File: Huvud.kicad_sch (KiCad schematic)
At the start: 117 parts, among them J10 Probe, J12 5V, J2 DBG, J3 THERM, J4 FAN0, J5 FAN1, J6 Heater, J7 Endstop, J9 STEPPER, Q1 AO3400A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

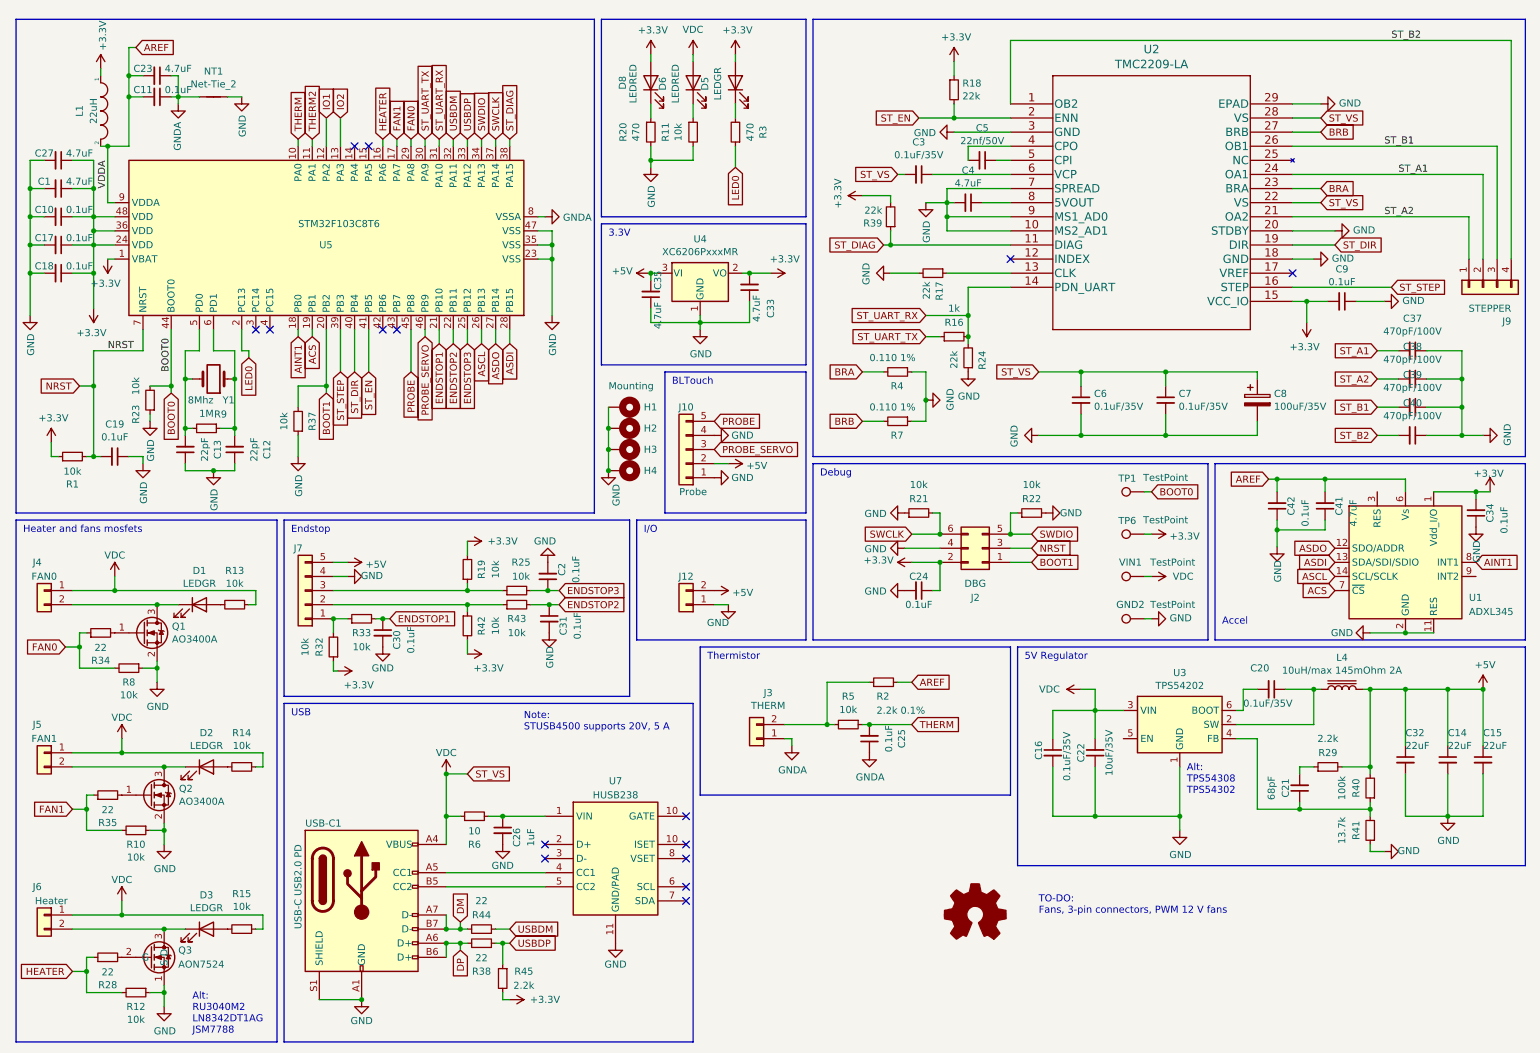
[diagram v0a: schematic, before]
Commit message: repace TMC2209 with module
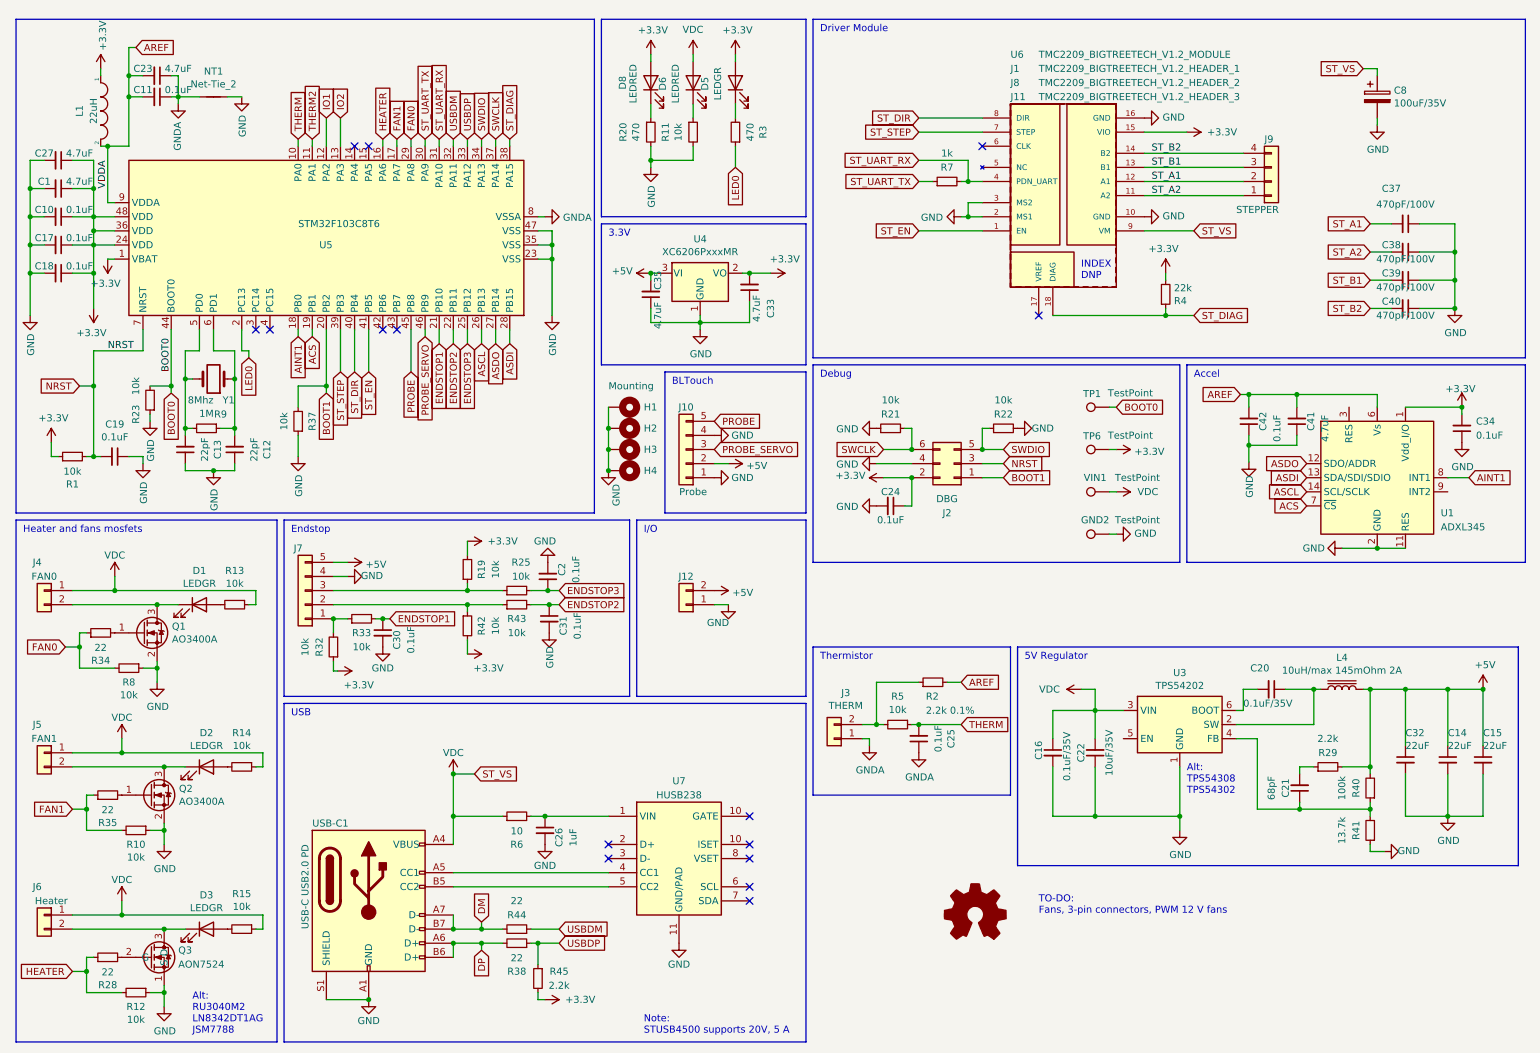
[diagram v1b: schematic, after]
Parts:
- removed C3, C6, C7: 0.1uF/35V, Capacitor_SMD:C_0603_1608Metric, symbol Device:C_Small
- removed C4: 4.7uF, Capacitor_SMD:C_0402_1005Metric, symbol Device:C_Small
- removed C5: 22nf/50V, Capacitor_SMD:C_0603_1608Metric, symbol Device:C_Small
- removed C9: 0.1uF, Capacitor_SMD:C_0402_1005Metric, symbol Device:C_Small
- removed R16: 1k, Resistor_SMD:R_0402_1005Metric, symbol Device:R_Small
- removed R17, R18, R24, R39: 22k, Resistor_SMD:R_0402_1005Metric, symbol Device:R_Small
- removed U2: TMC2209-LA, TMC2209:TMC2209-LA, symbol TMC2209:TMC2209-LA
- added J1: TMC2209_BIGTREETECH_V1.2_HEADER_1, Huvud:HEADER_TMC2209_BIGTREETECH_1, symbol Huvud:TMC2209_BIGTREETECH_V1.2_HEADER_1
- added J11: TMC2209_BIGTREETECH_V1.2_HEADER_3, Huvud:HEADER_TMC2209_BIGTREETECH_3, symbol Huvud:TMC2209_BIGTREETECH_V1.2_HEADER_3
- added J8: TMC2209_BIGTREETECH_V1.2_HEADER_2, Huvud:HEADER_TMC2209_BIGTREETECH_2, symbol Huvud:TMC2209_BIGTREETECH_V1.2_HEADER_2
- added U6: TMC2209_BIGTREETECH_V1.2_MODULE, Huvud:MODULE_TMC2209_BIGTREETECH, symbol Huvud:TMC2209_BIGTREETECH_V1.2_MODULE
- R4: value 0.110 1% -> 22k; footprint Resistor_SMD:R_1206_3216Metric -> Resistor_SMD:R_0402_1005Metric; LCSC (none) -> C25768
- R7: value 0.110 1% -> 1k; footprint Resistor_SMD:R_1206_3216Metric -> Resistor_SMD:R_0402_1005Metric; LCSC (none) -> C21190
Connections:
- net BRA is gone; now on net +3V3: R4.2
- net BRB is gone; now on net ST_UART_RX: R7.2
- net +3V3: now also J8.15 (VIO)
- net GND: now also J1.2 (MS1), J1.3 (MS2), J8.10 (GND), J8.16 (GND); no longer R4.1, R7.1
- net ST_A1: now also J8.12 (A1)
- net ST_A2: now also J8.11 (A2)
- net ST_B1: now also J8.13 (B1)
- net ST_B2: now also J8.14 (B2)
- net ST_DIAG: now also R4.1, J11.18 (DIAG)
- net ST_DIR: now also J1.8 (DIR)
- net ST_EN: now also J1.1 (EN)
- net ST_STEP: now also J1.7 (STEP)
- net ST_UART_RX: now also J1.4 (PDN_UART)
- net ST_UART_TX: now also R7.1
- net VDC: now also J8.9 (VM)
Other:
- note added: "Driver Module"
- note added: "INDEX DNP"
- moved on the sheet: C24, C25, C26, C34, C37, C38, C39, C40, C41, C42, C8, GND2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

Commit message: cleanup and bom
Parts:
- GND2, H1, H2, H3, H4, TP1, TP6, VIN1: now left out of the parts list
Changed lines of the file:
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@@
   )
   (symbol (lib_id "Mechanical:MountingHole_Pad") (at 121.92 82.55 270) (unit 1)
-    (in_bom yes) (on_board yes) (dnp no)
+    (in_bom no) (on_board yes) (dnp no)
     (property "Reference" "H1" (at 125.73 82.55 90)
       (effects (font (size 1.27 1.27)) (justify left))
@@
   )
   (symbol (lib_id "Mechanical:MountingHole_Pad") (at 121.92 86.36 270) (unit 1)
-    (in_bom yes) (on_board yes) (dnp no)
+    (in_bom no) (on_board yes) (dnp no)
     (property "Reference" "H2" (at 125.73 86.36 90)
       (effects (font (size 1.27 1.27)) (justify left))
@@
   )
   (symbol (lib_id "Mechanical:MountingHole_Pad") (at 121.92 90.17 270) (unit 1)
-    (in_bom yes) (on_board yes) (dnp no)
+    (in_bom no) (on_board yes) (dnp no)
     (property "Reference" "H3" (at 125.73 90.17 90)
       (effects (font (size 1.27 1.27)) (justify left))
@@
   )
   (symbol (lib_id "Mechanical:MountingHole_Pad") (at 121.92 93.98 270) (unit 1)
-    (in_bom yes) (on_board yes) (dnp no)
+    (in_bom no) (on_board yes) (dnp no)
     (property "Reference" "H4" (at 125.73 93.98 90)
       (effects (font (size 1.27 1.27)) (justify left))
@@
   )
   (symbol (lib_id "Connector:TestPoint") (at 209.55 82.55 90) (unit 1)
-    (in_bom yes) (on_board yes) (dnp no)
+    (in_bom no) (on_board yes) (dnp no)
     (property "Reference" "TP1" (at 206.4512 80.137 90)
       (effects (font (size 1.27 1.27)))
@@
   )
   (symbol (lib_id "Connector:TestPoint") (at 209.55 90.17 90) (unit 1)
-    (in_bom yes) (on_board yes) (dnp no)
+    (in_bom no) (on_board yes) (dnp no)
     (property "Reference" "TP6" (at 206.4512 87.757 90)
       (effects (font (size 1.27 1.27)))
@@
   )
   (symbol (lib_id "Connector:TestPoint") (at 209.55 105.41 90) (unit 1)
-    (in_bom yes) (on_board yes) (dnp no)
+    (in_bom no) (on_board yes) (dnp no)
     (property "Reference" "GND2" (at 207.01 102.87 90)
       (effects (font (size 1.27 1.27)))
@@
   )
   (symbol (lib_id "Connector:TestPoint") (at 209.55 97.79 90) (unit 1)
-    (in_bom yes) (on_board yes) (dnp no)
+    (in_bom no) (on_board yes) (dnp no)
     (property "Reference" "VIN1" (at 207.01 95.25 90)
       (effects (font (size 1.27 1.27)))
